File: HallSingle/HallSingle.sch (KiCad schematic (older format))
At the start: 10 parts, among them J1 Conn_01x03, U1 SS49E, U2 TS331ILT

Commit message: Added Voron Logo and filled missing resistor value
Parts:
- R3: value R -> 1k
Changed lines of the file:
@@
 P 5700 2250
 F 0 "R3" H 5770 2296 50  0000 L CNN
-F 1 "R" H 5770 2205 50  0000 L CNN
+F 1 "1k" H 5770 2205 50  0000 L CNN
 F 2 "HallEffect:R_0805_2012Metric" V 5630 2250 50  0001 C CNN
 F 3 "~" H 5700 2250 50  0001 C CNN

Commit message: Reduced size due to almost certain interferance from screw heads on v1.8 Y.
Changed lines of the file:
@@
 	3100 2500 3450 2500
 Connection ~ 3100 2500
-Wire Wire Line
-	3100 2200 3100 2150
 $Comp
 L HallEffect:C C1
@@
 $EndComp
 Connection ~ 3100 2800
-Wire Wire Line
-	2950 1950 2950 2150
-Wire Wire Line
-	2950 2150 3100 2150
-Connection ~ 3100 2150
-Wire Wire Line
-	3100 2150 3100 2100
 $Comp
 L power:+5V #PWR01
@@
 Text Notes 2300 2250 0    50   ~ 0
 R1=1k R2=10k\nVmax=4.545\nVmin=2.381
+Wire Wire Line
+	3100 2100 3100 2150
+Wire Wire Line
+	2950 1950 2950 2150
+Wire Wire Line
+	2950 2150 3100 2150
+Connection ~ 3100 2150
+Wire Wire Line
+	3100 2150 3100 2200
 $EndSCHEMATC

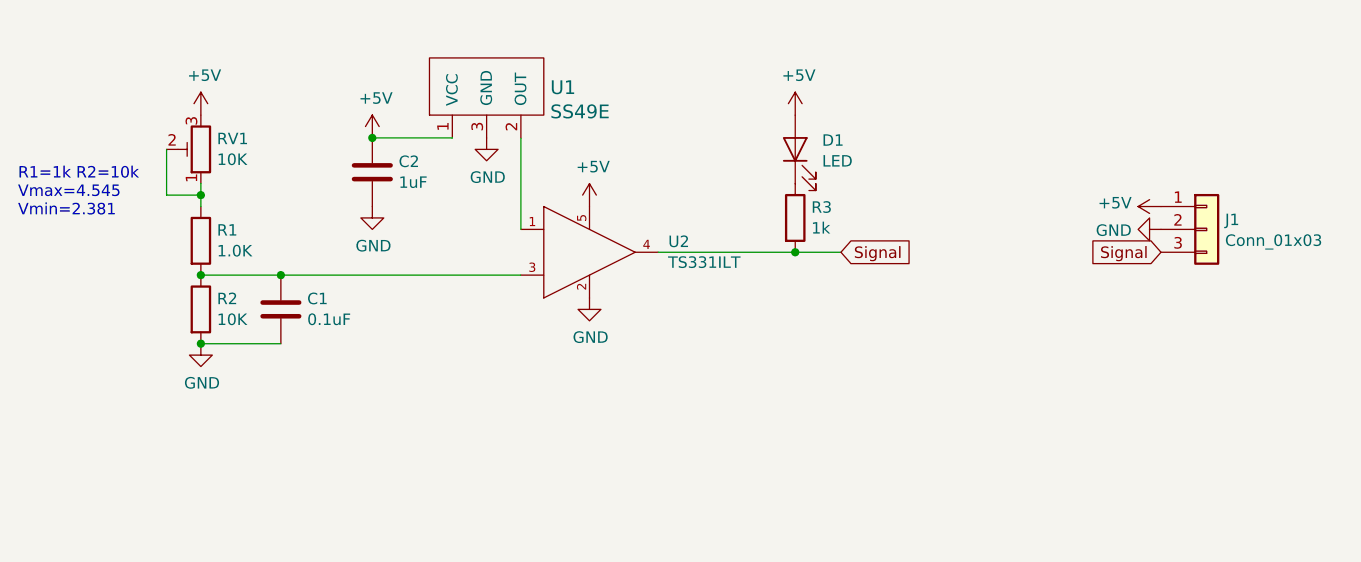
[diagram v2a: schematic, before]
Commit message: Changed comparator to reverse - also NOTed  the led. this is to help with fault tolerance
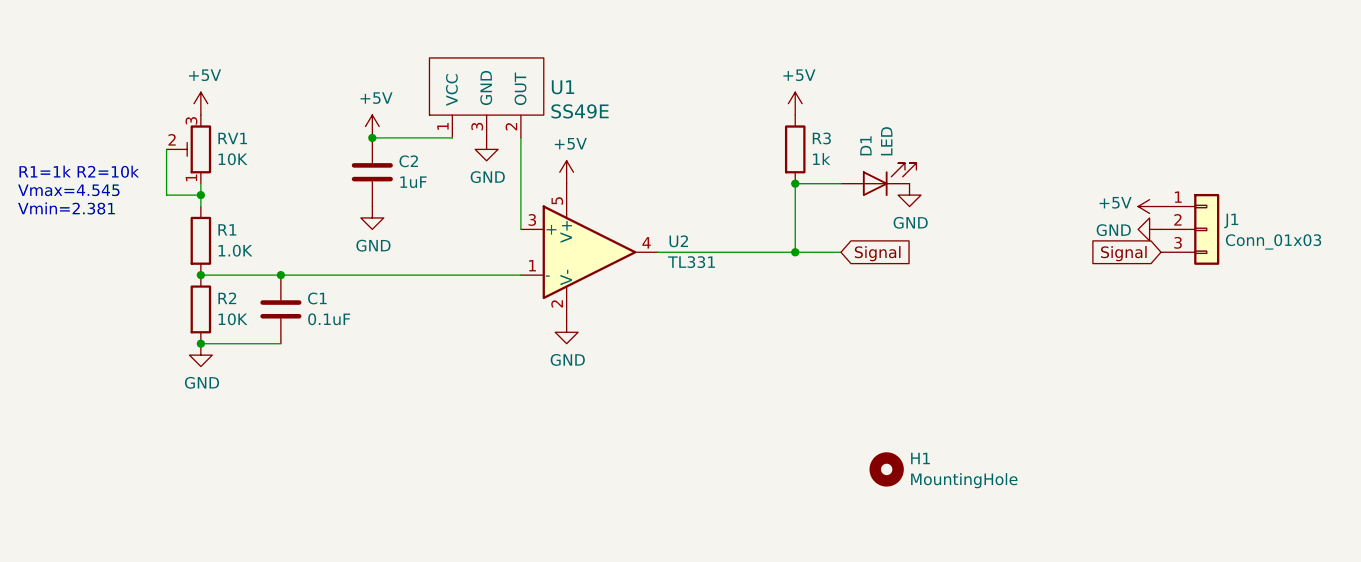
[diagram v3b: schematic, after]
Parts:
- removed U2: TS331ILT, HallEffect:SOT-23-5, symbol HallEffect:TS331ILT
- added H1: MountingHole, HallEffect:MountingHole_3.2mm_M3, symbol HallEffect:MountingHole
- added U2: TL331, Package_TO_SOT_SMD:SOT-23-5, symbol Comparator:TL331
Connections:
- net +5V: now also R3.1, U2.5 (V+); no longer D1.2 (A)
- net GND: now also D1.1 (K), U2.2 (V-)
- net Signal: now also D1.2 (A), U2.4
- net at U1.2 (OUT): now also U2.3 (+)
- net at C1.1, R1.2, R2.1: now also U2.1 (-)
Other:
- moved on the sheet: D1, R3
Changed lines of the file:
@@
 Signal
-$Comp
-L HallEffect:TS331ILT U2
-U 1 1 5FEA1D5C
-P 4400 2300
-F 0 "U2" H 5144 2246 50  0000 L CNN
-F 1 "TS331ILT" H 5144 2155 50  0000 L CNN
-F 2 "HallEffect:SOT-23-5" H 4400 2700 50  0001 L CNN
-F 3 "https://www.st.com/resource/en/datasheet/ts331.pdf" H 4400 2800 50  0001 L CNN
-F 4 "IC" H 4400 2900 50  0001 L CNN "category"
-F 5 "Integrated Circuits (ICs)" H 4400 3000 50  0001 L CNN "device class L1"
-F 6 "Linear ICs" H 4400 3100 50  0001 L CNN "device class L2"
-F 7 "Comparators" H 4400 3200 50  0001 L CNN "device class L3"
-F 8 "IC COMPARATOR SINGLE SOT23-5" H 4400 3300 50  0001 L CNN "digikey description"
-F 9 "497-10555-1-ND" H 4400 3400 50  0001 L CNN "digikey part number"
-F 10 "1.45mm" H 4400 3500 50  0001 L CNN "height"
-F 11 "0.03uA" H 4400 3600 50  0001 L CNN "input bias current"
-F 12 "0.5mV" H 4400 3700 50  0001 L CNN "input offset voltage"
-F 13 "SOT95P280X120-5" H 4400 3800 50  0001 L CNN "ipc land pattern name"
-F 14 "yes" H 4400 3900 50  0001 L CNN "lead free"
-F 15 "bbb9eb91c0aa956b" H 4400 4000 50  0001 L CNN "library id"
-F 16 "STMicroelectronics" H 4400 4100 50  0001 L CNN "manufacturer"
-F 17 "+150°C" H 4400 4200 50  0001 L CNN "max junction temp"
-F 18 "5V" H 4400 4300 50  0001 L CNN "max supply voltage"
-F 19 "1.6V" H 4400 4400 50  0001 L CNN "min supply voltage"
-F 20 "Analog Comparators Micropower 20uA 1.6V to 5V RtoR" H 4400 4500 50  0001 L CNN "mouser description"
-F 21 "511-TS331ILT" H 4400 4600 50  0001 L CNN "mouser part number"
-F 22 "23-26uA" H 4400 4700 50  0001 L CNN "nominal supply current"
-F 23 "1" H 4400 4800 50  0001 L CNN "number of channels"
-F 24 "93mA" H 4400 4900 50  0001 L CNN "output current per channel"
-F 25 "SOT23-5" H 4400 5000 50  0001 L CNN "package"
-F 26 "yes" H 4400 5100 50  0001 L CNN "rohs"
-F 27 "+125°C" H 4400 5200 50  0001 L CNN "temperature range high"
-F 28 "-40°C" H 4400 5300 50  0001 L CNN "temperature range low"
-	1    4400 2300
-	1    0    0    -1
-$EndComp
 $Comp
 L power:GND #PWR07
 U 1 1 5FEA2C66
-P 4800 2600
-F 0 "#PWR07" H 4800 2350 50  0001 C CNN
-F 1 "GND" H 4805 2427 50  0000 C CNN
-F 2 "" H 4800 2600 50  0001 C CNN
-F 3 "" H 4800 2600 50  0001 C CNN
-	1    4800 2600
+P 4700 2700
+F 0 "#PWR07" H 4700 2450 50  0001 C CNN
+F 1 "GND" H 4705 2527 50  0000 C CNN
+F 2 "" H 4700 2700 50  0001 C CNN
+F 3 "" H 4700 2700 50  0001 C CNN
+	1    4700 2700
 	1    0    0    -1
 $EndComp
@@
 L power:+5V #PWR06
 U 1 1 5FEA32F8
-P 4800 2200
-F 0 "#PWR06" H 4800 2050 50  0001 C CNN
-F 1 "+5V" H 4815 2373 50  0000 C CNN
-F 2 "" H 4800 2200 50  0001 C CNN
-F 3 "" H 4800 2200 50  0001 C CNN
-	1    4800 2200
+P 4700 2100
+F 0 "#PWR06" H 4700 1950 50  0001 C CNN
+F 1 "+5V" H 4715 2273 50  0000 C CNN
+F 2 "" H 4700 2100 50  0001 C CNN
+F 3 "" H 4700 2100 50  0001 C CNN
+	1    4700 2100
 	1    0    0    -1
 $EndComp
@@
 L HallEffect:R R3
 U 1 1 5FEB5185
-P 5700 2250
-F 0 "R3" H 5770 2296 50  0000 L CNN
-F 1 "1k" H 5770 2205 50  0000 L CNN
-F 2 "HallEffect:R_0805_2012Metric" V 5630 2250 50  0001 C CNN
-F 3 "~" H 5700 2250 50  0001 C CNN
-	1    5700 2250
+P 5700 1950
+F 0 "R3" H 5770 1996 50  0000 L CNN
+F 1 "1k" H 5770 1905 50  0000 L CNN
+F 2 "HallEffect:R_0805_2012Metric" V 5630 1950 50  0001 C CNN
+F 3 "~" H 5700 1950 50  0001 C CNN
+	1    5700 1950
 	1    0    0    -1
 $EndComp
@@
 L Device:LED D1
 U 1 1 5FEB5CD2
-P 5700 1950
-F 0 "D1" V 5739 1833 50  0000 R CNN
-F 1 "LED" V 5648 1833 50  0000 R CNN
-F 2 "HallEffect:LED_0805_2012Metric" H 5700 1950 50  0001 C CNN
-F 3 "~" H 5700 1950 50  0001 C CNN
-	1    5700 1950
-	0    -1   -1   0
+P 6050 2100
+F 0 "D1" V 6089 1983 50  0000 R CNN
+F 1 "LED" V 5998 1983 50  0000 R CNN
+F 2 "HallEffect:LED_0805_2012Metric" H 6050 2100 50  0001 C CNN
+F 3 "~" H 6050 2100 50  0001 C CNN
+	1    6050 2100
+	-1   0    0    1
 $EndComp
 $Comp
@@
 Text GLabel 5900 2400 2    50   Input ~ 0
 Signal
-Wire Wire Line
-	5100 2400 5700 2400
-Connection ~ 5700 2400
-Wire Wire Line
-	5700 2400 5900 2400
 Text Notes 2300 2250 0    50   ~ 0
 R1=1k R2=10k\nVmax=4.545\nVmin=2.381
@@
 Wire Wire Line
 	3100 2150 3100 2200
+Wire Wire Line
+	5100 2400 5700 2400
+$Comp
+L power:GND #PWR011
+U 1 1 6007DD31
+P 6200 2100
+F 0 "#PWR011" H 6200 1850 50  0001 C CNN
+F 1 "GND" H 6205 1927 50  0000 C CNN
+F 2 "" H 6200 2100 50  0001 C CNN
+F 3 "" H 6200 2100 50  0001 C CNN
+	1    6200 2100
+	1    0    0    -1
+$EndComp
+Wire Wire Line
+	5900 2100 5700 2100
+Wire Wire Line
+	5700 2100 5700 2400
+Connection ~ 5700 2100
+Connection ~ 5700 2400
+Wire Wire Line
+	5700 2400 5900 2400
+$Comp
+L Comparator:TL331 U2
+U 1 1 6007B14C
+P 4800 2400
+F 0 "U2" H 5144 2446 50  0000 L CNN
+F 1 "TL331" H 5144 2355 50  0000 L CNN
+F 2 "Package_TO_SOT_SMD:SOT-23-5" H 4850 1800 50  0001 C CNN
+F 3 "http://www.ti.com/lit/ds/symlink/tl331.pdf" H 4800 2600 50  0001 C CNN
+	1    4800 2400
+	1    0    0    -1
+$EndComp
+$Comp
+L HallEffect:MountingHole H1
+U 1 1 60082DD5
+P 6100 3350
+F 0 "H1" H 6200 3396 50  0000 L CNN
+F 1 "MountingHole" H 6200 3305 50  0000 L CNN
+F 2 "HallEffect:MountingHole_3.2mm_M3" H 6100 3350 50  0001 C CNN
+F 3 "~" H 6100 3350 50  0001 C CNN
+	1    6100 3350
+	1    0    0    -1
+$EndComp
 $EndSCHEMATC

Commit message: Corrected wiring to comparator to NC config. Updated header to be same config as SKR - straight through cable required. update revision number
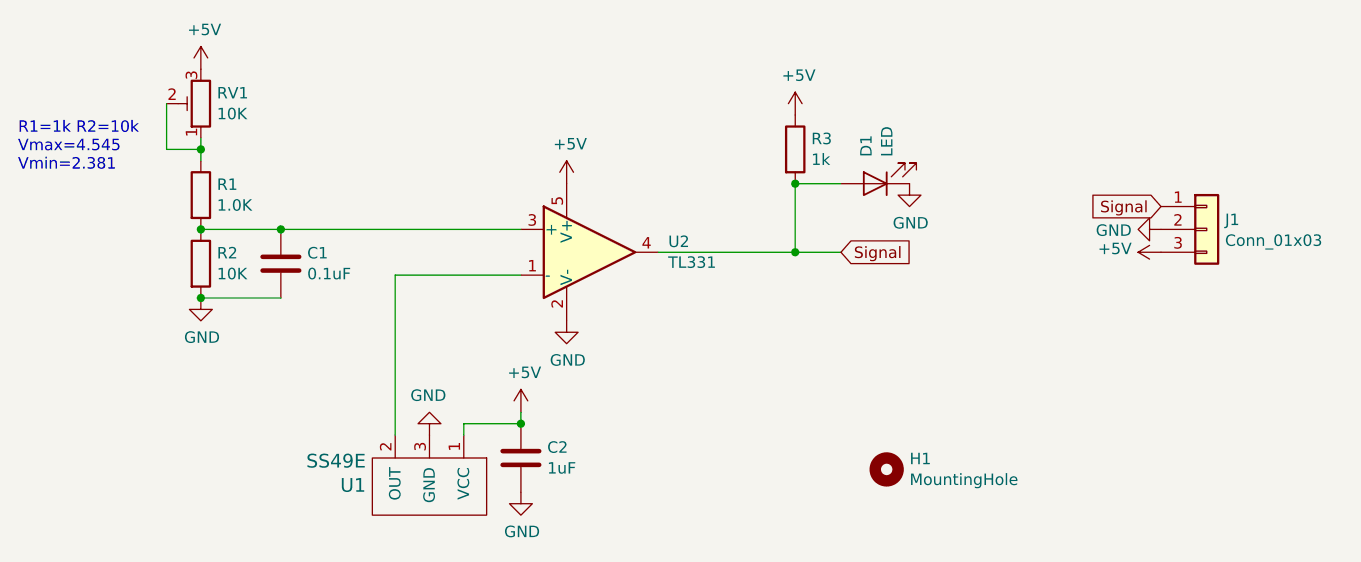
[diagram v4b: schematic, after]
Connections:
- net +5V: now also J1.3 (Pin_3); no longer J1.1 (Pin_1)
- net Signal: now also J1.1 (Pin_1); no longer J1.3 (Pin_3)
- net at U1.2 (OUT): now also U2.1 (-); no longer U2.3 (+)
- net at C1.1, R1.2, R2.1: now also U2.3 (+); no longer U2.1 (-)
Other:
- moved on the sheet: C1, C2, R1, R2, RV1, U1
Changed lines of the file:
@@
 L power:+5V #PWR09
 U 1 1 5FE9D08F
-P 7300 2200
-F 0 "#PWR09" H 7300 2050 50  0001 C CNN
-F 1 "+5V" V 7315 2328 50  0000 L CNN
-F 2 "" H 7300 2200 50  0001 C CNN
-F 3 "" H 7300 2200 50  0001 C CNN
-	1    7300 2200
+P 7300 2400
+F 0 "#PWR09" H 7300 2250 50  0001 C CNN
+F 1 "+5V" V 7315 2528 50  0000 L CNN
+F 2 "" H 7300 2400 50  0001 C CNN
+F 3 "" H 7300 2400 50  0001 C CNN
+	1    7300 2400
 	0    -1   -1   0
 $EndComp
-Text GLabel 7300 2400 0    50   Input ~ 0
+Text GLabel 7300 2200 0    50   Input ~ 0
 Signal
 $Comp
@@
 L HallEffect:SS49E U1
 U 1 1 5FEA3EB5
-P 4350 1800
-F 0 "U1" H 4628 1920 60  0000 L CNN
-F 1 "SS49E" H 4628 1814 60  0000 L CNN
-F 2 "HallEffect:SOT-23" H 4250 1800 60  0001 C CNN
-F 3 "" H 4250 1800 60  0001 C CNN
-	1    4350 1800
-	1    0    0    -1
+P 4100 3300
+F 0 "U1" H 4378 3420 60  0000 L CNN
+F 1 "SS49E" H 4378 3314 60  0000 L CNN
+F 2 "HallEffect:SOT-23" H 4000 3300 60  0001 C CNN
+F 3 "" H 4000 3300 60  0001 C CNN
+	1    4100 3300
+	-1   0    0    1
 $EndComp
 $Comp
 L power:GND #PWR05
 U 1 1 5FEA483D
-P 4350 1900
-F 0 "#PWR05" H 4350 1650 50  0001 C CNN
-F 1 "GND" H 4355 1727 50  0000 C CNN
-F 2 "" H 4350 1900 50  0001 C CNN
-F 3 "" H 4350 1900 50  0001 C CNN
-	1    4350 1900
-	1    0    0    -1
-$EndComp
-Wire Wire Line
-	4200 1900 3850 1900
-$Comp
-L power:+5V #PWR03
-U 1 1 5FEA5973
-P 3850 1900
-F 0 "#PWR03" H 3850 1750 50  0001 C CNN
-F 1 "+5V" H 3865 2073 50  0000 C CNN
-F 2 "" H 3850 1900 50  0001 C CNN
-F 3 "" H 3850 1900 50  0001 C CNN
-	1    3850 1900
-	1    0    0    -1
-$EndComp
-$Comp
-L power:GND #PWR04
-U 1 1 5FEA5FC6
-P 3850 2200
-F 0 "#PWR04" H 3850 1950 50  0001 C CNN
-F 1 "GND" H 3855 2027 50  0000 C CNN
-F 2 "" H 3850 2200 50  0001 C CNN
-F 3 "" H 3850 2200 50  0001 C CNN
-	1    3850 2200
-	1    0    0    -1
-$EndComp
-Wire Wire Line
-	4500 1900 4500 2300
+P 4100 3200
+F 0 "#PWR05" H 4100 2950 50  0001 C CNN
+F 1 "GND" H 4105 3027 50  0000 C CNN
+F 2 "" H 4100 3200 50  0001 C CNN
+F 3 "" H 4100 3200 50  0001 C CNN
+	1    4100 3200
+	-1   0    0    1
+$EndComp
 $Comp
 L HallEffect:R R2
 U 1 1 5FEADFC8
-P 3100 2650
-F 0 "R2" H 3170 2696 50  0000 L CNN
-F 1 "10K" H 3170 2605 50  0000 L CNN
-F 2 "HallEffect:R_0805_2012Metric" V 3030 2650 50  0001 C CNN
-F 3 "~" H 3100 2650 50  0001 C CNN
-	1    3100 2650
+P 3100 2450
+F 0 "R2" H 3170 2496 50  0000 L CNN
+F 1 "10K" H 3170 2405 50  0000 L CNN
+F 2 "HallEffect:R_0805_2012Metric" V 3030 2450 50  0001 C CNN
+F 3 "~" H 3100 2450 50  0001 C CNN
+	1    3100 2450
 	1    0    0    -1
 $EndComp
@@
 L HallEffect:R R1
 U 1 1 5FEAE921
-P 3100 2350
-F 0 "R1" H 3170 2396 50  0000 L CNN
-F 1 "1.0K" H 3170 2305 50  0000 L CNN
-F 2 "HallEffect:R_0805_2012Metric" V 3030 2350 50  0001 C CNN
-F 3 "~" H 3100 2350 50  0001 C CNN
-	1    3100 2350
-	1    0    0    -1
-$EndComp
-Connection ~ 3850 1900
-$Comp
-L HallEffect:C C2
-U 1 1 5FEAD587
-P 3850 2050
-F 0 "C2" H 3965 2096 50  0000 L CNN
-F 1 "1uF" H 3965 2005 50  0000 L CNN
-F 2 "HallEffect:C_0805_2012Metric" H 3888 1900 50  0001 C CNN
-F 3 "~" H 3850 2050 50  0001 C CNN
-	1    3850 2050
+P 3100 2150
+F 0 "R1" H 3170 2196 50  0000 L CNN
+F 1 "1.0K" H 3170 2105 50  0000 L CNN
+F 2 "HallEffect:R_0805_2012Metric" V 3030 2150 50  0001 C CNN
+F 3 "~" H 3100 2150 50  0001 C CNN
+	1    3100 2150
 	1    0    0    -1
 $EndComp
@@
 L Device:R_POT_TRIM RV1
 U 1 1 5FEAFE4B
-P 3100 1950
-F 0 "RV1" H 3030 1904 50  0000 R CNN
-F 1 "10K" H 3030 1995 50  0000 R CNN
-F 2 "HallEffect:CT6EP103" H 3100 1950 50  0001 C CNN
-F 3 "~" H 3100 1950 50  0001 C CNN
-	1    3100 1950
-	-1   0    0    1
-$EndComp
-Wire Wire Line
-	3100 2500 3450 2500
-Connection ~ 3100 2500
+P 3100 1750
+F 0 "RV1" H 3030 1704 50  0000 R CNN
+F 1 "10K" H 3030 1795 50  0000 R CNN
+F 2 "HallEffect:CT6EP103" H 3100 1750 50  0001 C CNN
+F 3 "~" H 3100 1750 50  0001 C CNN
+	1    3100 1750
+	-1   0    0    1
+$EndComp
+Wire Wire Line
+	3100 2300 3450 2300
+Connection ~ 3100 2300
 $Comp
 L HallEffect:C C1
 U 1 1 5FEB3165
-P 3450 2650
-F 0 "C1" H 3565 2696 50  0000 L CNN
-F 1 "0.1uF" H 3565 2605 50  0000 L CNN
-F 2 "HallEffect:C_0805_2012Metric" H 3488 2500 50  0001 C CNN
-F 3 "~" H 3450 2650 50  0001 C CNN
-	1    3450 2650
-	1    0    0    -1
-$EndComp
-Connection ~ 3450 2500
-Wire Wire Line
-	3450 2500 4500 2500
-Wire Wire Line
-	3450 2800 3100 2800
+P 3450 2450
+F 0 "C1" H 3565 2496 50  0000 L CNN
+F 1 "0.1uF" H 3565 2405 50  0000 L CNN
+F 2 "HallEffect:C_0805_2012Metric" H 3488 2300 50  0001 C CNN
+F 3 "~" H 3450 2450 50  0001 C CNN
+	1    3450 2450
+	1    0    0    -1
+$EndComp
+Connection ~ 3450 2300
+Wire Wire Line
+	3450 2300 4500 2300
+Wire Wire Line
+	3450 2600 3100 2600
 $Comp
 L power:GND #PWR02
 U 1 1 5FEB3CBB
-P 3100 2800
-F 0 "#PWR02" H 3100 2550 50  0001 C CNN
-F 1 "GND" H 3105 2627 50  0000 C CNN
-F 2 "" H 3100 2800 50  0001 C CNN
-F 3 "" H 3100 2800 50  0001 C CNN
-	1    3100 2800
-	1    0    0    -1
-$EndComp
-Connection ~ 3100 2800
+P 3100 2600
+F 0 "#PWR02" H 3100 2350 50  0001 C CNN
+F 1 "GND" H 3105 2427 50  0000 C CNN
+F 2 "" H 3100 2600 50  0001 C CNN
+F 3 "" H 3100 2600 50  0001 C CNN
+	1    3100 2600
+	1    0    0    -1
+$EndComp
+Connection ~ 3100 2600
 $Comp
 L power:+5V #PWR01
 U 1 1 5FEB4703
-P 3100 1800
-F 0 "#PWR01" H 3100 1650 50  0001 C CNN
-F 1 "+5V" H 3115 1973 50  0000 C CNN
-F 2 "" H 3100 1800 50  0001 C CNN
-F 3 "" H 3100 1800 50  0001 C CNN
-	1    3100 1800
+P 3100 1600
+F 0 "#PWR01" H 3100 1450 50  0001 C CNN
+F 1 "+5V" H 3115 1773 50  0000 C CNN
+F 2 "" H 3100 1600 50  0001 C CNN
+F 3 "" H 3100 1600 50  0001 C CNN
+	1    3100 1600
 	1    0    0    -1
 $EndComp
@@
 Text GLabel 5900 2400 2    50   Input ~ 0
 Signal
-Text Notes 2300 2250 0    50   ~ 0
+Text Notes 2300 2050 0    50   ~ 0
 R1=1k R2=10k\nVmax=4.545\nVmin=2.381
 Wire Wire Line
-	3100 2100 3100 2150
-Wire Wire Line
-	2950 1950 2950 2150
-Wire Wire Line
-	2950 2150 3100 2150
-Connection ~ 3100 2150
-Wire Wire Line
-	3100 2150 3100 2200
+	3100 1900 3100 1950
+Wire Wire Line
+	2950 1750 2950 1950
+Wire Wire Line
+	2950 1950 3100 1950
+Connection ~ 3100 1950
+Wire Wire Line
+	3100 1950 3100 2000
 Wire Wire Line
 	5100 2400 5700 2400
@@
 	5700 2400 5900 2400
 $Comp
+L HallEffect:MountingHole H1
+U 1 1 60082DD5
+P 6100 3350
+F 0 "H1" H 6200 3396 50  0000 L CNN
+F 1 "MountingHole" H 6200 3305 50  0000 L CNN
+F 2 "HallEffect:MountingHole_3.2mm_M3" H 6100 3350 50  0001 C CNN
+F 3 "~" H 6100 3350 50  0001 C CNN
+	1    6100 3350
+	1    0    0    -1
+$EndComp
+$Comp
 L Comparator:TL331 U2
 U 1 1 6007B14C
@@
 $EndComp
 $Comp
-L HallEffect:MountingHole H1
-U 1 1 60082DD5
-P 6100 3350
-F 0 "H1" H 6200 3396 50  0000 L CNN
-F 1 "MountingHole" H 6200 3305 50  0000 L CNN
-F 2 "HallEffect:MountingHole_3.2mm_M3" H 6100 3350 50  0001 C CNN
-F 3 "~" H 6100 3350 50  0001 C CNN
-	1    6100 3350
-	1    0    0    -1
-$EndComp
+L HallEffect:C C2
+U 1 1 5FEAD587
+P 4500 3300
+F 0 "C2" H 4615 3346 50  0000 L CNN
+F 1 "1uF" H 4615 3255 50  0000 L CNN
+F 2 "HallEffect:C_0805_2012Metric" H 4538 3150 50  0001 C CNN
+F 3 "~" H 4500 3300 50  0001 C CNN
+	1    4500 3300
+	1    0    0    -1
+$EndComp
+$Comp
+L power:GND #PWR04
+U 1 1 5FEA5FC6
+P 4500 3450
+F 0 "#PWR04" H 4500 3200 50  0001 C CNN
+F 1 "GND" H 4505 3277 50  0000 C CNN
+F 2 "" H 4500 3450 50  0001 C CNN
+F 3 "" H 4500 3450 50  0001 C CNN
+	1    4500 3450
+	1    0    0    -1
+$EndComp
+$Comp
+L power:+5V #PWR03
+U 1 1 5FEA5973
+P 4500 3100
+F 0 "#PWR03" H 4500 2950 50  0001 C CNN
+F 1 "+5V" H 4515 3273 50  0000 C CNN
+F 2 "" H 4500 3100 50  0001 C CNN
+F 3 "" H 4500 3100 50  0001 C CNN
+	1    4500 3100
+	1    0    0    -1
+$EndComp
+Wire Wire Line
+	4500 3150 4500 3100
+Wire Wire Line
+	4500 3150 4250 3150
+Wire Wire Line
+	4250 3150 4250 3200
+Connection ~ 4500 3150
+Wire Wire Line
+	3950 3200 3950 2500
+Wire Wire Line
+	3950 2500 4500 2500
 $EndSCHEMATC
